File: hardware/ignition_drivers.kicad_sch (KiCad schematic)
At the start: 29 parts, among them Q1 ISL9V3040D3STV, Q2 ISL9V3040D3STV, Q3 ISL9V3040D3STV, Q4 ISL9V3040D3STV, Q5 DMC2990UDJ, Q6 DMC2990UDJ, Q9 DMC2990UDJ, U10 ISO6740F-Q1, U11 ISO6740F-Q1, U12 SN6505BDBV-Q1, U14 DAC8551IxDGK, U15 OPA4376

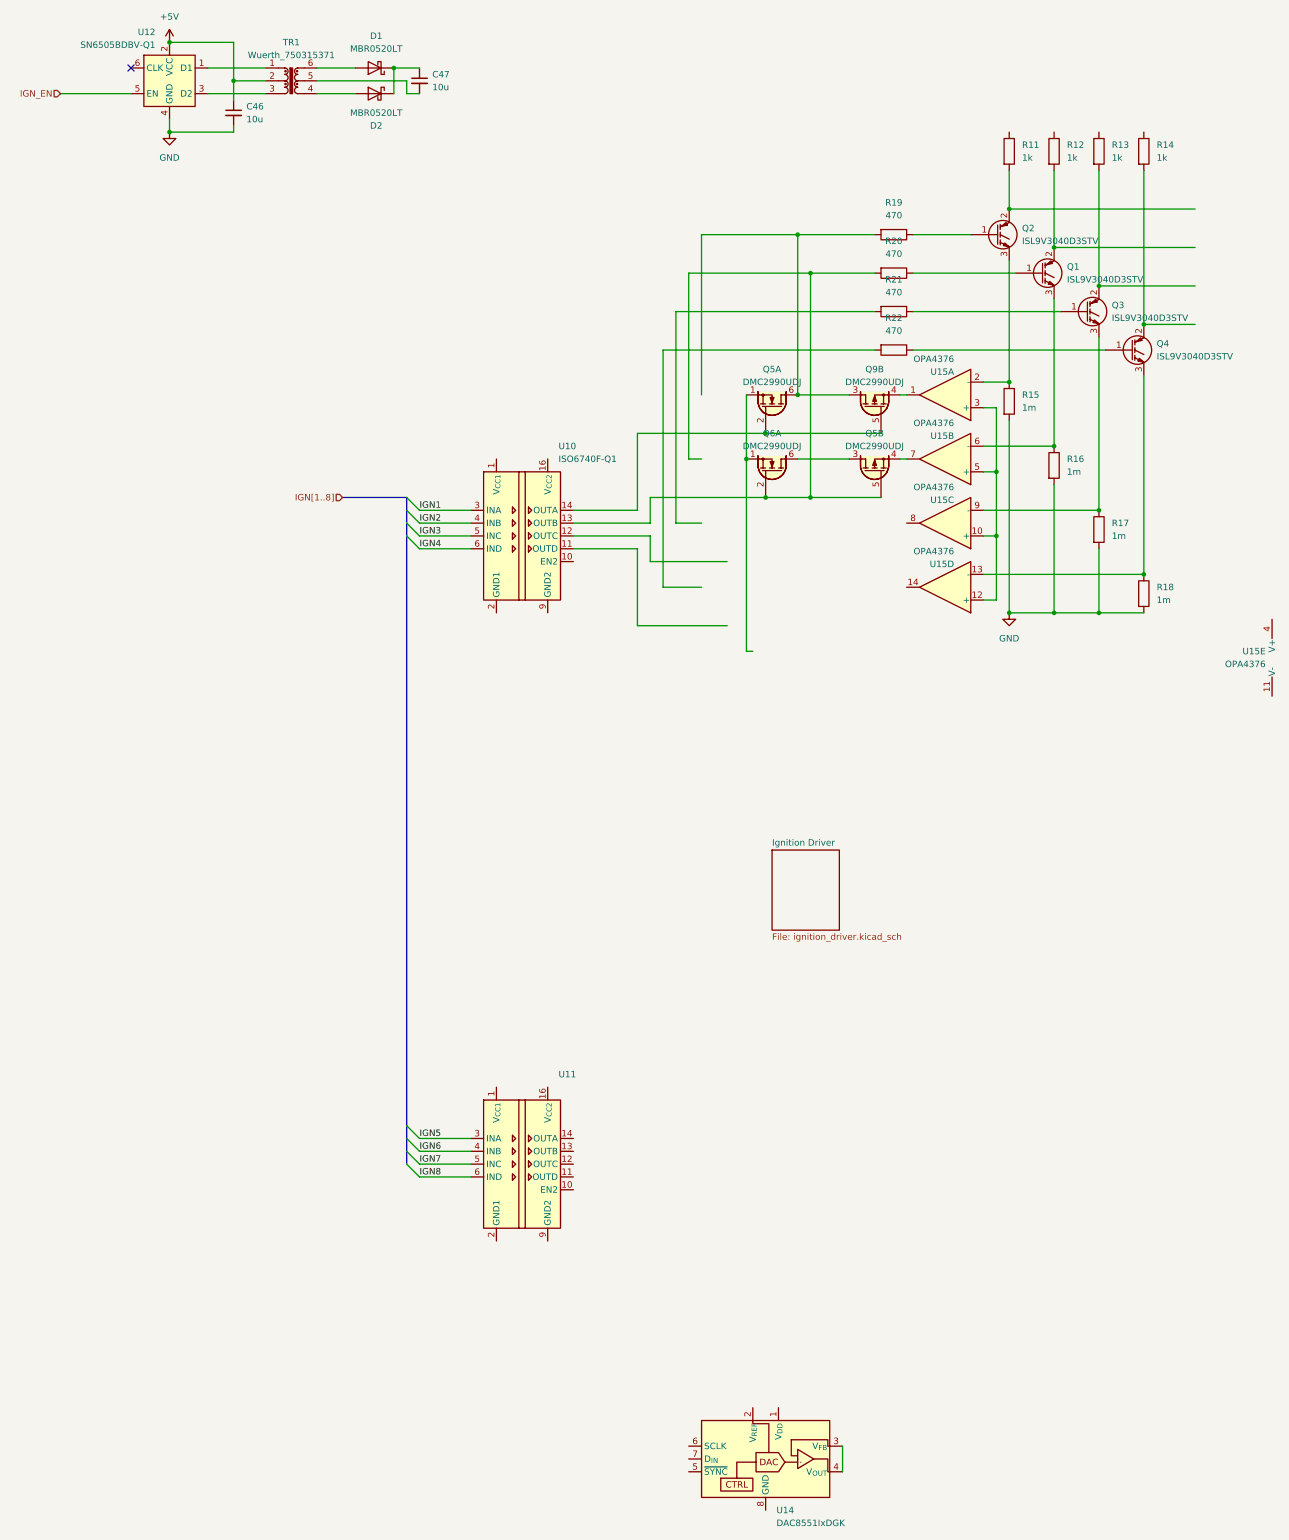
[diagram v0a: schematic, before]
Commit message: Finished preliminary IGN driver
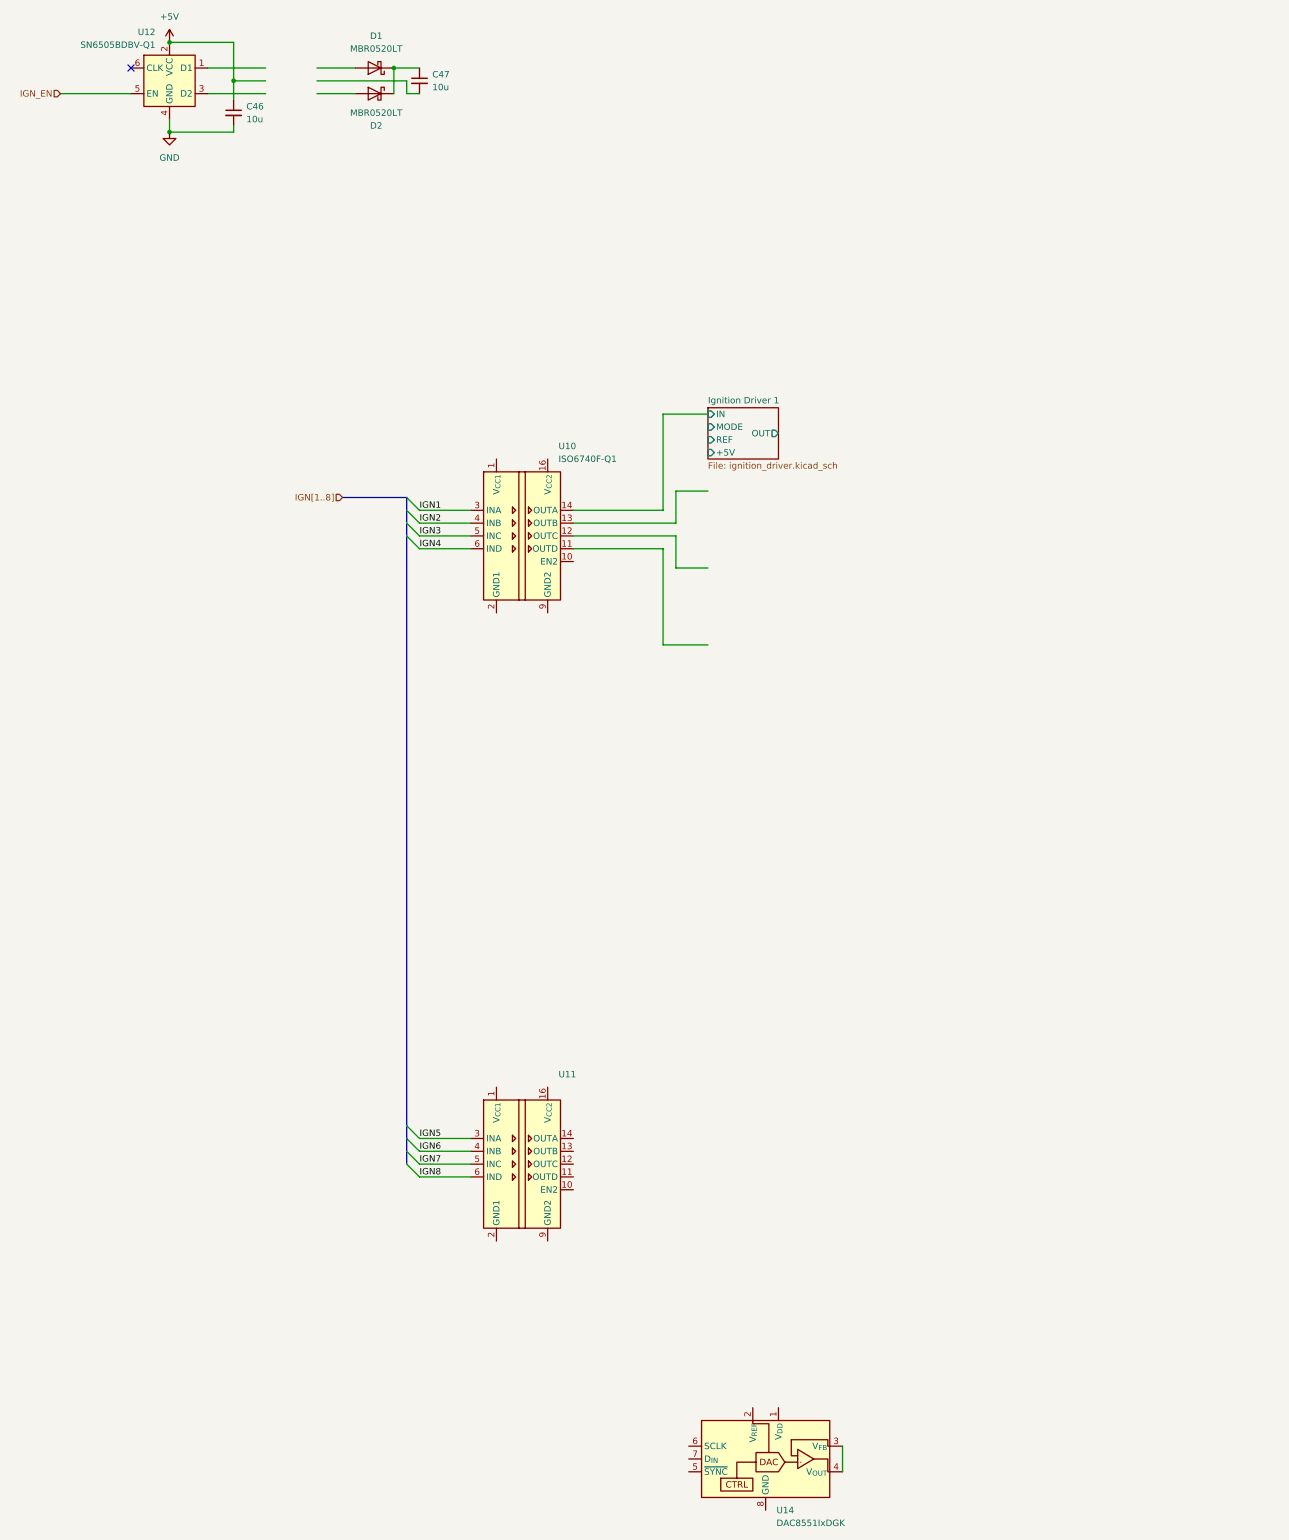
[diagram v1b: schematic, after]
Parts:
- removed Q1, Q2, Q3, Q4: ISL9V3040D3STV, Package_TO_SOT_SMD:TO-252-3_TabPin2, symbol Device:Q_NIGBT_GCE
- removed Q5, Q6, Q9: DMC2990UDJ, PCM_Package_TO_SOT_SMD_AKL:SOT-963, symbol PCM_Transistor_MOSFET_AKL:DMC2990UDJ
- removed R11, R12, R13, R14: 1k, symbol Device:R
- removed R15, R16, R17, R18: 1m, symbol Device:R
- removed R19, R20, R21, R22: 470, symbol Device:R
- removed TR1: Wuerth_750315371, Transformer_SMD:Transformer_Wuerth_750315371, symbol Transformer:Wuerth_750315371
- removed U15: OPA4376, symbol Amplifier_Operational:OPA4376
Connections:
- net Ignition Driver 1/IN: now reaches U10.14 (OUTA)
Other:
- sheet Ignition Driver renamed Ignition Driver 1
- sheet Ignition Driver 1 ports: added +5V, IN, MODE, OUT, REF; removed none
